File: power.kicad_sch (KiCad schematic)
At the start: 22 parts, among them U1 AP62150WU, U3 TLV75533PDBV, U4 USBLC6-2SC6

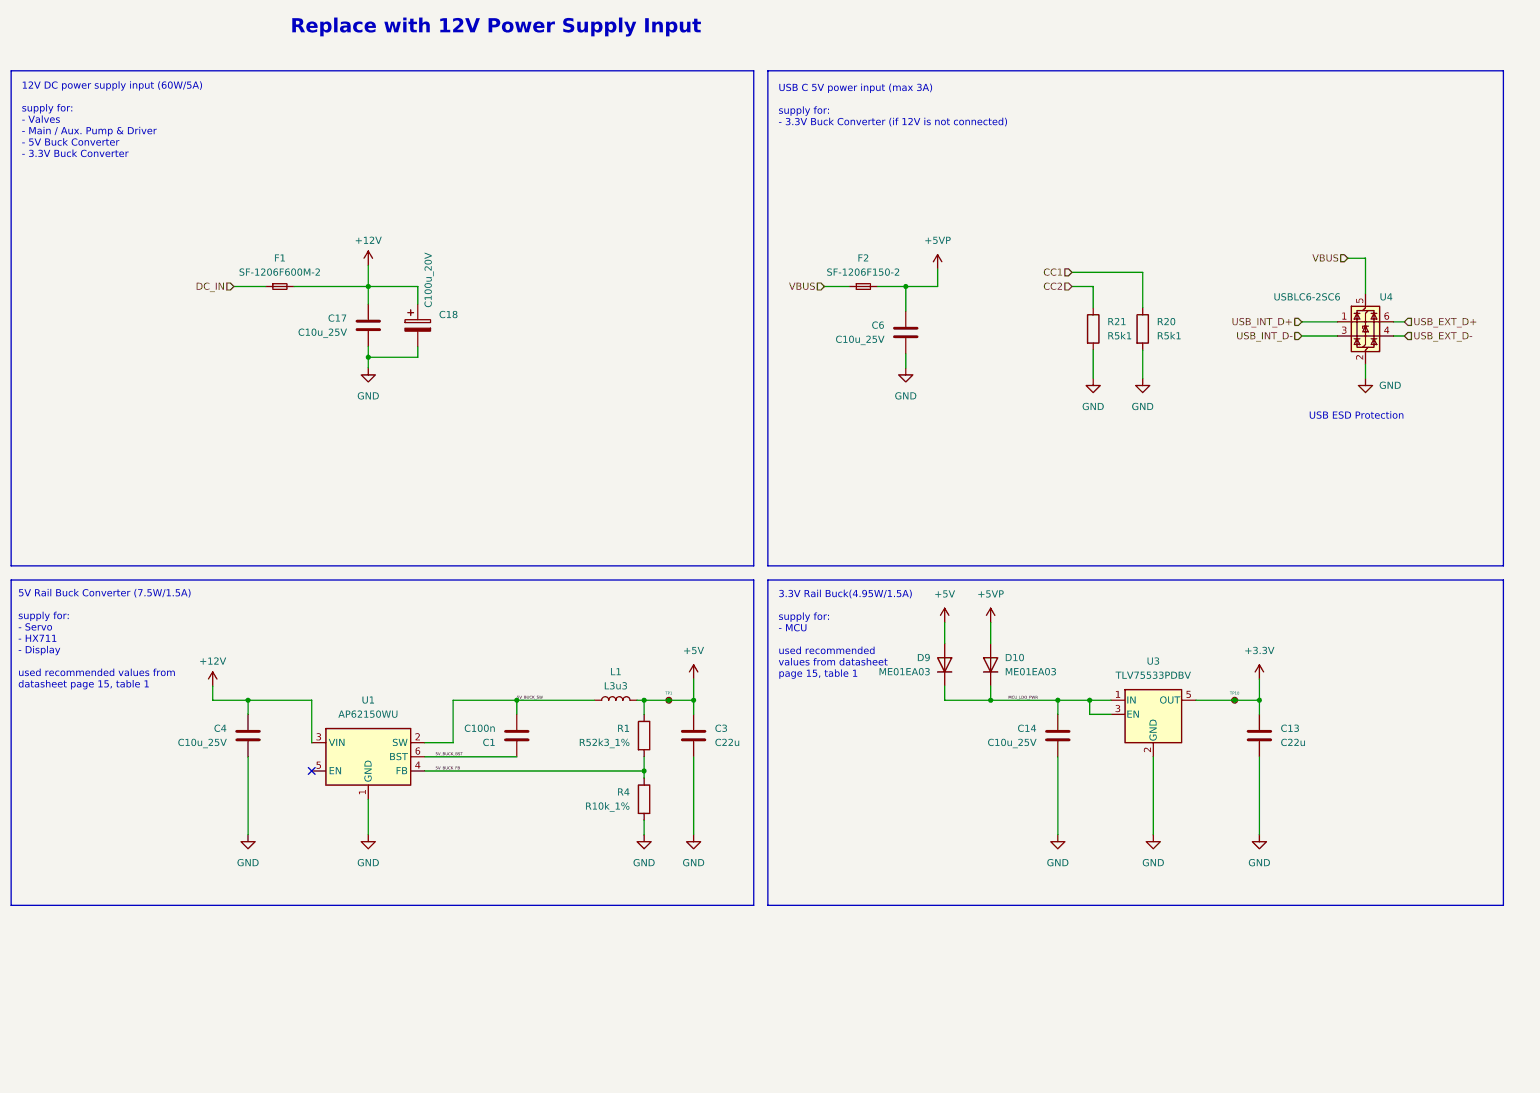
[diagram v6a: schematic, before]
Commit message: Reannotate geographically by layout
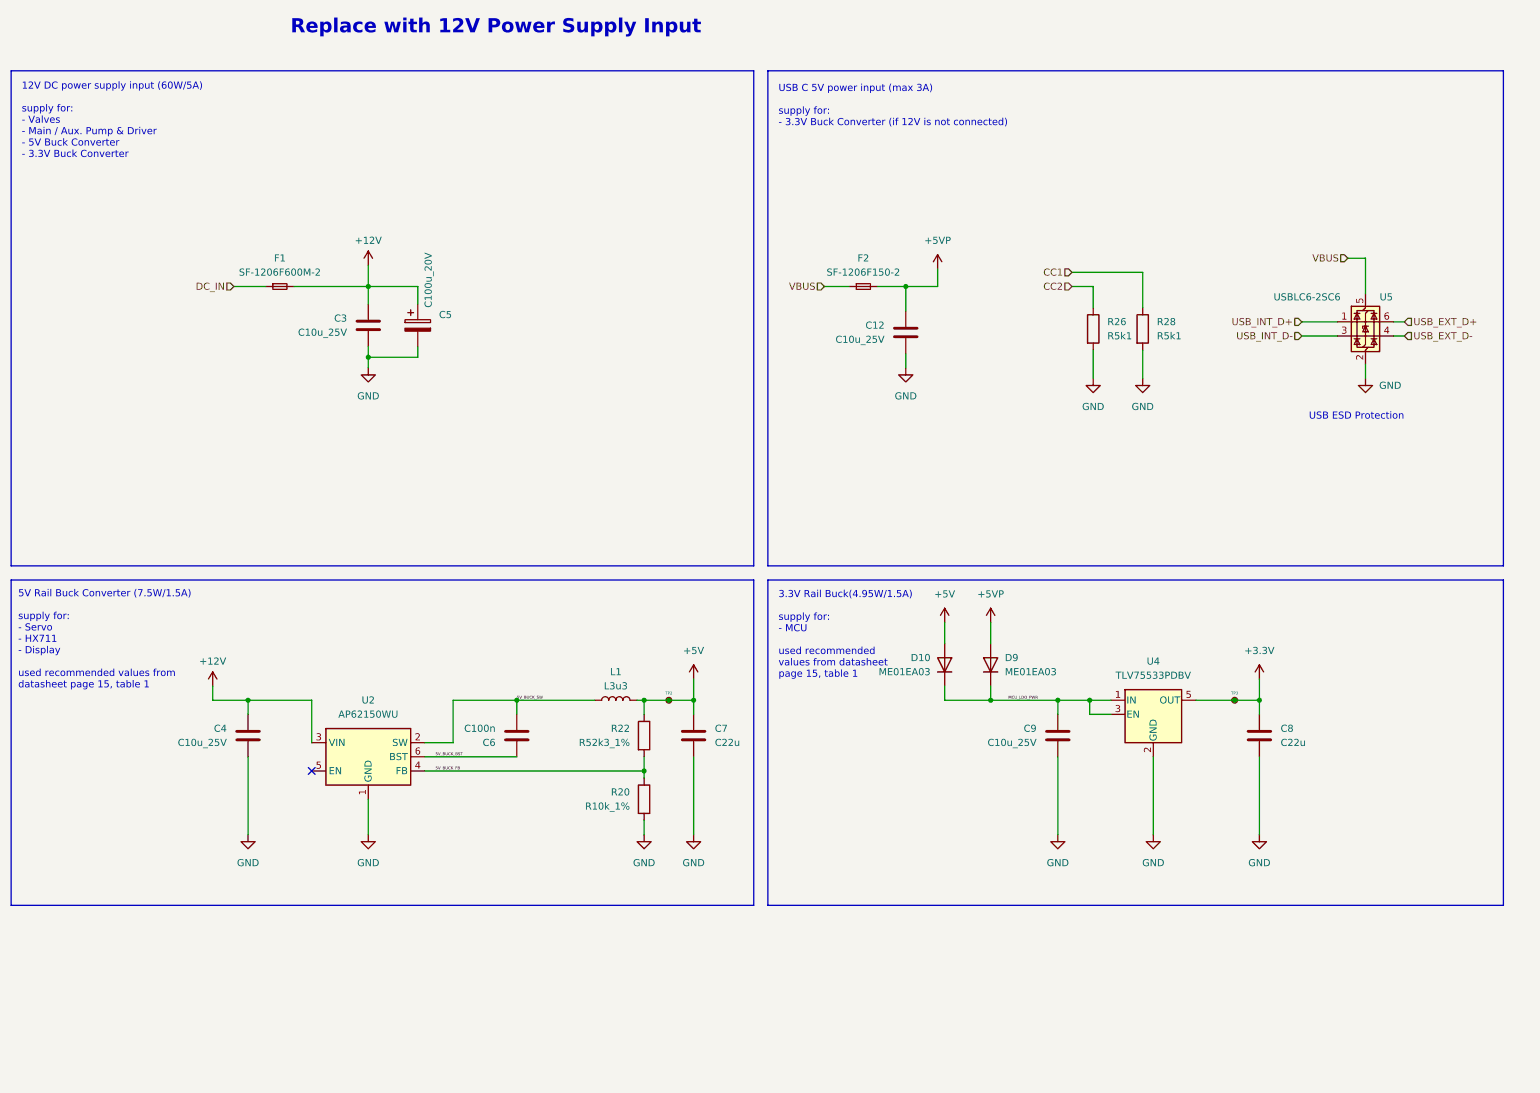
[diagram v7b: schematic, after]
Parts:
- renumbered C6 to C12, C17 to C3, C18 to C5, C1 to C6, C3 to C7, C13 to C8, C14 to C9, D9 to D10, D10 to D9, R4 to R20, R1 to R22, R21 to R26, R20 to R28, TP1 to TP2, TP10 to TP3, U1 to U2, U3 to U4, U4 to U5

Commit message: Final checks and cleanup
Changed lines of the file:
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@@
     (title "openautolab - Mainboard")
     (date "2024-04-03")
-    (rev "1.0")
+    (rev "2.0")
   )
   (junction (at 207.645 127) (diameter 0) (color 0 0 0 0)
   )
+  (junction (at 219.075 143.51) (diameter 0) (color 0 0 0 0)
+  )
   (junction (at 174.625 52.705) (diameter 0) (color 0 0 0 0)
   )
@@
   )
   (junction (at 127.635 139.7) (diameter 0) (color 0 0 0 0)
+  )
+  (junction (at 238.125 143.51) (diameter 0) (color 0 0 0 0)
   )
   (junction (at 78.105 52.705) (diameter 0) (color 0 0 0 0)
@@
     (stroke (width 0) (type default))
   )
+  (wire (pts (xy 238.125 143.51) (xy 238.125 151.13))
+    (stroke (width 0) (type default))
+  )
   (wire (pts (xy 174.625 52.705) (xy 174.625 57.15))
     (stroke (width 0) (type default))
@@
     (stroke (width 0) (type default))
   )
-  (wire (pts (xy 201.93 137.16) (xy 201.93 151.13))
-    (stroke (width 0) (type default))
-  )
   (wire (pts (xy 181.61 124.46) (xy 181.61 127))
     (stroke (width 0) (type default))
@@
     (stroke (width 0) (type default))
   )
-  (wire (pts (xy 219.075 137.16) (xy 219.075 151.13))
-    (stroke (width 0) (type default))
-  )
   (wire (pts (xy 181.61 127) (xy 189.865 127))
     (stroke (width 0) (type default))
@@
     (stroke (width 0) (type default))
   )
+  (wire (pts (xy 219.075 143.51) (xy 238.125 143.51))
+    (stroke (width 0) (type default))
+  )
   (wire (pts (xy 174.625 52.705) (xy 180.34 52.705))
     (stroke (width 0) (type default))
@@
     (stroke (width 0) (type default))
   )
+  (wire (pts (xy 219.075 137.16) (xy 219.075 143.51))
+    (stroke (width 0) (type default))
+  )
   (wire (pts (xy 169.545 52.705) (xy 174.625 52.705))
     (stroke (width 0) (type default))
@@
     (stroke (width 0) (type default))
   )
+  (wire (pts (xy 201.93 137.16) (xy 201.93 143.51))
+    (stroke (width 0) (type default))
+  )
   (wire (pts (xy 254 47.625) (xy 257.175 47.625))
     (stroke (width 0) (type default))
   )
+  (wire (pts (xy 201.93 143.51) (xy 219.075 143.51))
+    (stroke (width 0) (type default))
+  )
   (wire (pts (xy 189.865 127) (xy 201.93 127))
     (stroke (width 0) (type default))
@@
     (stroke (width 0) (type default))
   )
+  (wire (pts (xy 238.125 137.16) (xy 238.125 143.51))
+    (stroke (width 0) (type default))
+  )
   (wire (pts (xy 136.525 127) (xy 136.525 129.54))
     (stroke (width 0) (type default))
@@
   )
   (wire (pts (xy 88.265 139.7) (xy 127.635 139.7))
-    (stroke (width 0) (type default))
-  )
-  (wire (pts (xy 238.125 137.16) (xy 238.125 151.13))
     (stroke (width 0) (type default))
   )
@@
         (path "/613f8c39-c37c-4981-8911-5138d36a7959/163d5f85-e35a-4492-902b-e1a6f214f674"
           (reference "R22") (unit 1)
-        )
-      )
-    )
-  )
-  (symbol (lib_id "power:GND") (at 201.93 151.13 0) (unit 1)
-    (in_bom yes) (on_board yes) (dnp no) (fields_autoplaced)
-    (property "Reference" "#PWR028" (at 201.93 157.48 0)
-      (effects (font (size 1.27 1.27)) hide)
-    )
-    (property "Value" "GND" (at 201.93 156.21 0)
-      (effects (font (size 1.27 1.27)))
-    )
-    (property "Footprint" "" (at 201.93 151.13 0)
-      (effects (font (size 1.27 1.27)) hide)
-    )
-    (property "Datasheet" "" (at 201.93 151.13 0)
-      (effects (font (size 1.27 1.27)) hide)
-    )
-    (pin "1")
-    (instances
-      (project "mainboard"
-        (path "/613f8c39-c37c-4981-8911-5138d36a7959/163d5f85-e35a-4492-902b-e1a6f214f674"
-          (reference "#PWR028") (unit 1)
         )
       )
@@
         )
       )
-    )
-  )
-  (symbol (lib_id "power:GND") (at 219.075 151.13 0) (unit 1)
-    (in_bom yes) (on_board yes) (dnp no) (fields_autoplaced)
-    (property "Reference" "#PWR011" (at 219.075 157.48 0)
-      (effects (font (size 1.27 1.27)) hide)
-    )
-    (property "Value" "GND" (at 219.075 156.21 0)
-      (effects (font (size 1.27 1.27)))
-    )
-    (property "Footprint" "" (at 219.075 151.13 0)
-      (effects (font (size 1.27 1.27)) hide)
-    )
-    (property "Datasheet" "" (at 219.075 151.13 0)
-      (effects (font (size 1.27 1.27)) hide)
-    )
-    (pin "1")
-    (instances
-      (project "mainboard"
-        (path "/613f8c39-c37c-4981-8911-5138d36a7959/163d5f85-e35a-4492-902b-e1a6f214f674"
-          (reference "#PWR011") (unit 1)
-        )
-      )
